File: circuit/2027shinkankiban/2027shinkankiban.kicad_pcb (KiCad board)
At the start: 2 copper layers, 22 parts, among them J1 Conn_01x02_Pin, U1 ATtiny44A-P, U2 MCP9700Ax-ETT

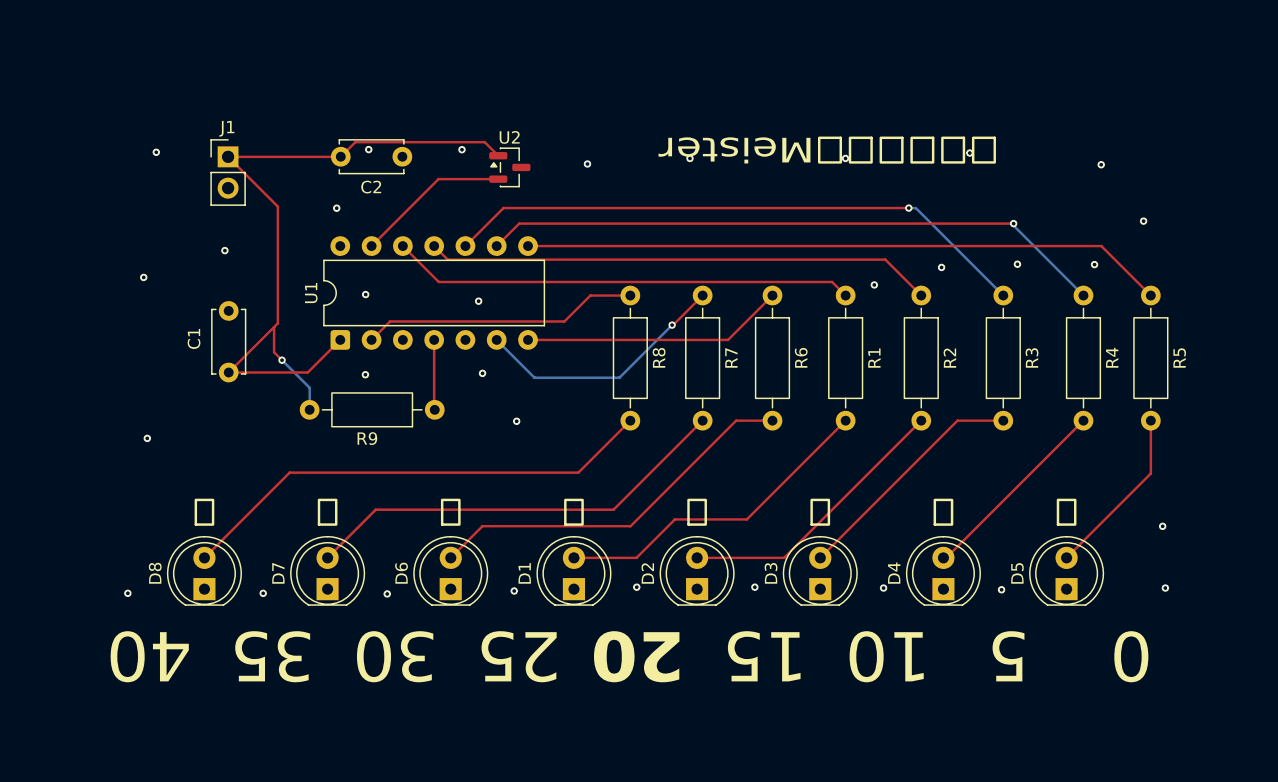
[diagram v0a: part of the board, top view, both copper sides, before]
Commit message: 2027年新歓用基板を追加
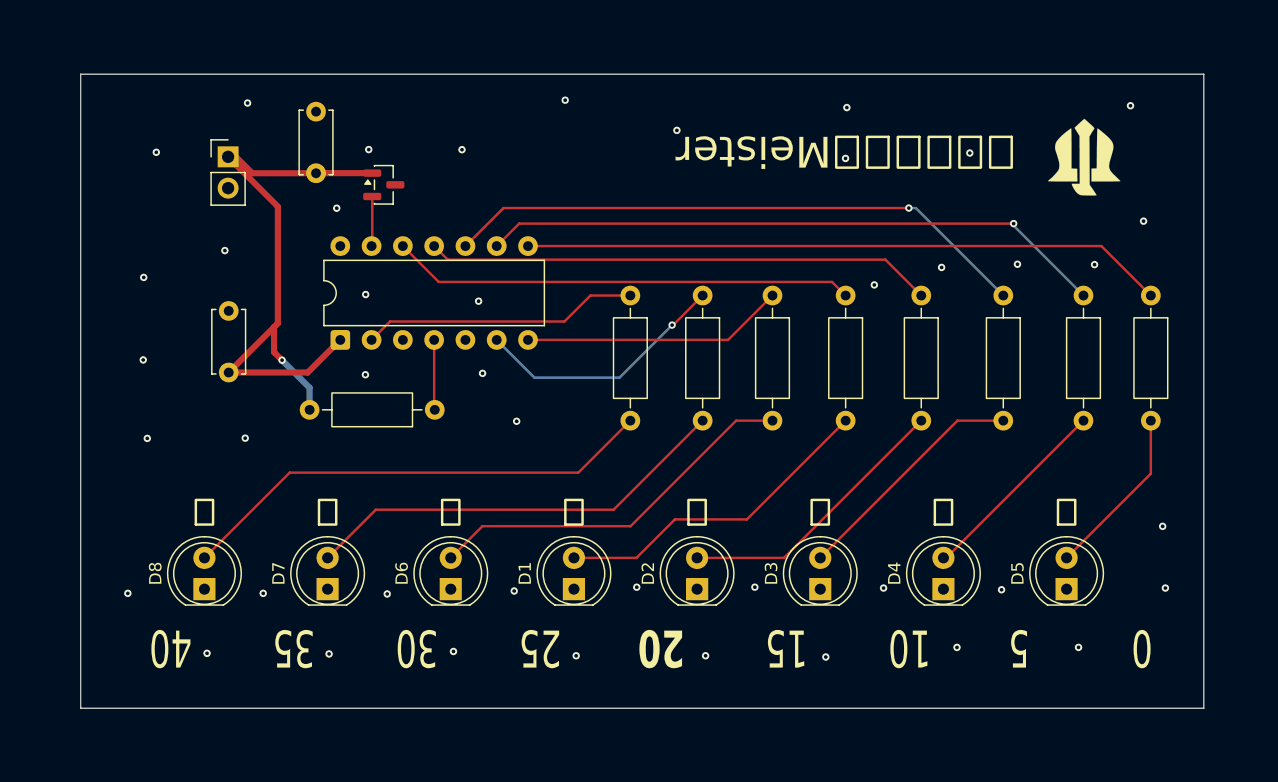
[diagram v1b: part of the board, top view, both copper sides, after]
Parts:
- added G***: LOGO, Meister:MeisterLogo, F.Cu at (194.3, 85.1)
- moved U2 10.3 mm to (137.6, 87.2)
- moved C2 7.91 mm to (132.1, 81.2), turned to -90 degrees
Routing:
- net VCC: track 61.8 -> 51.2 mm
- net Net-(U1-AREF/PA0): track 12.5 -> 4.05 mm
- net GND: vias 32 -> 45
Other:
- board outline added: 91.2 x 51.5 mm
